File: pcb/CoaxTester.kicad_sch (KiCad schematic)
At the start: 20 parts

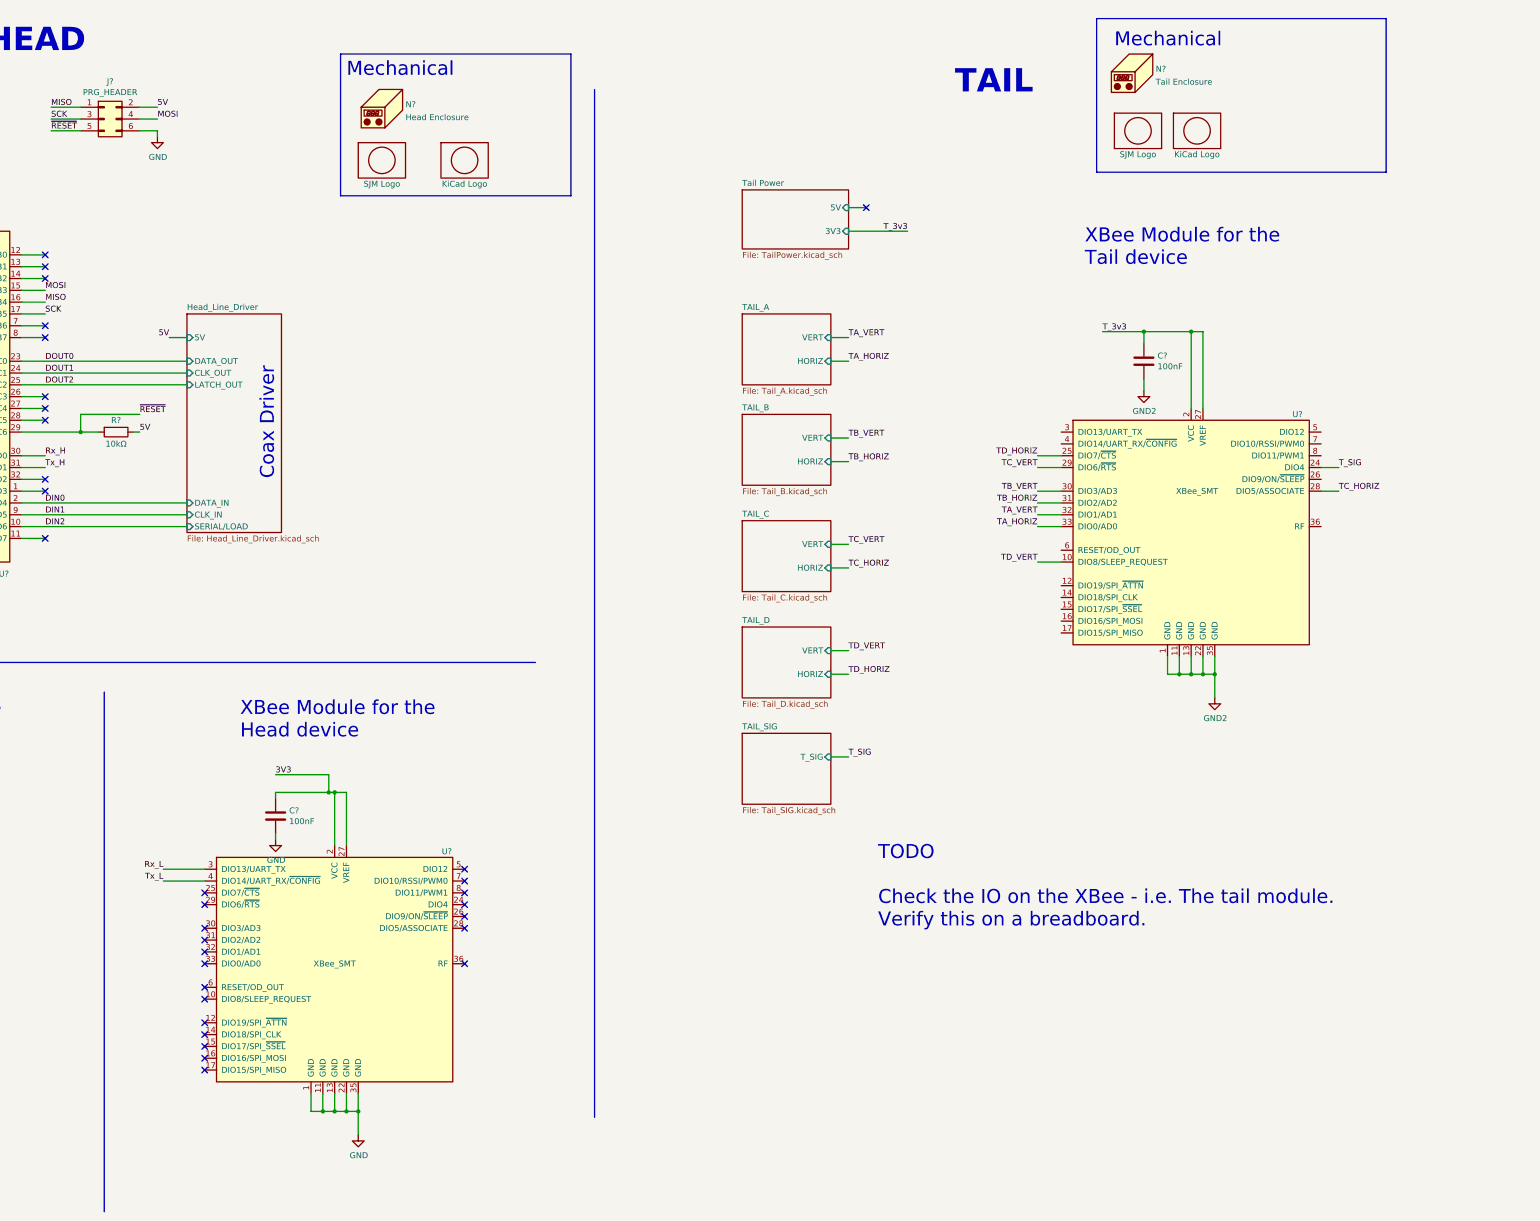
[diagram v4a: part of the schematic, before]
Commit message: Proof of concept for XBee tail unit. Correction to XBee symbol
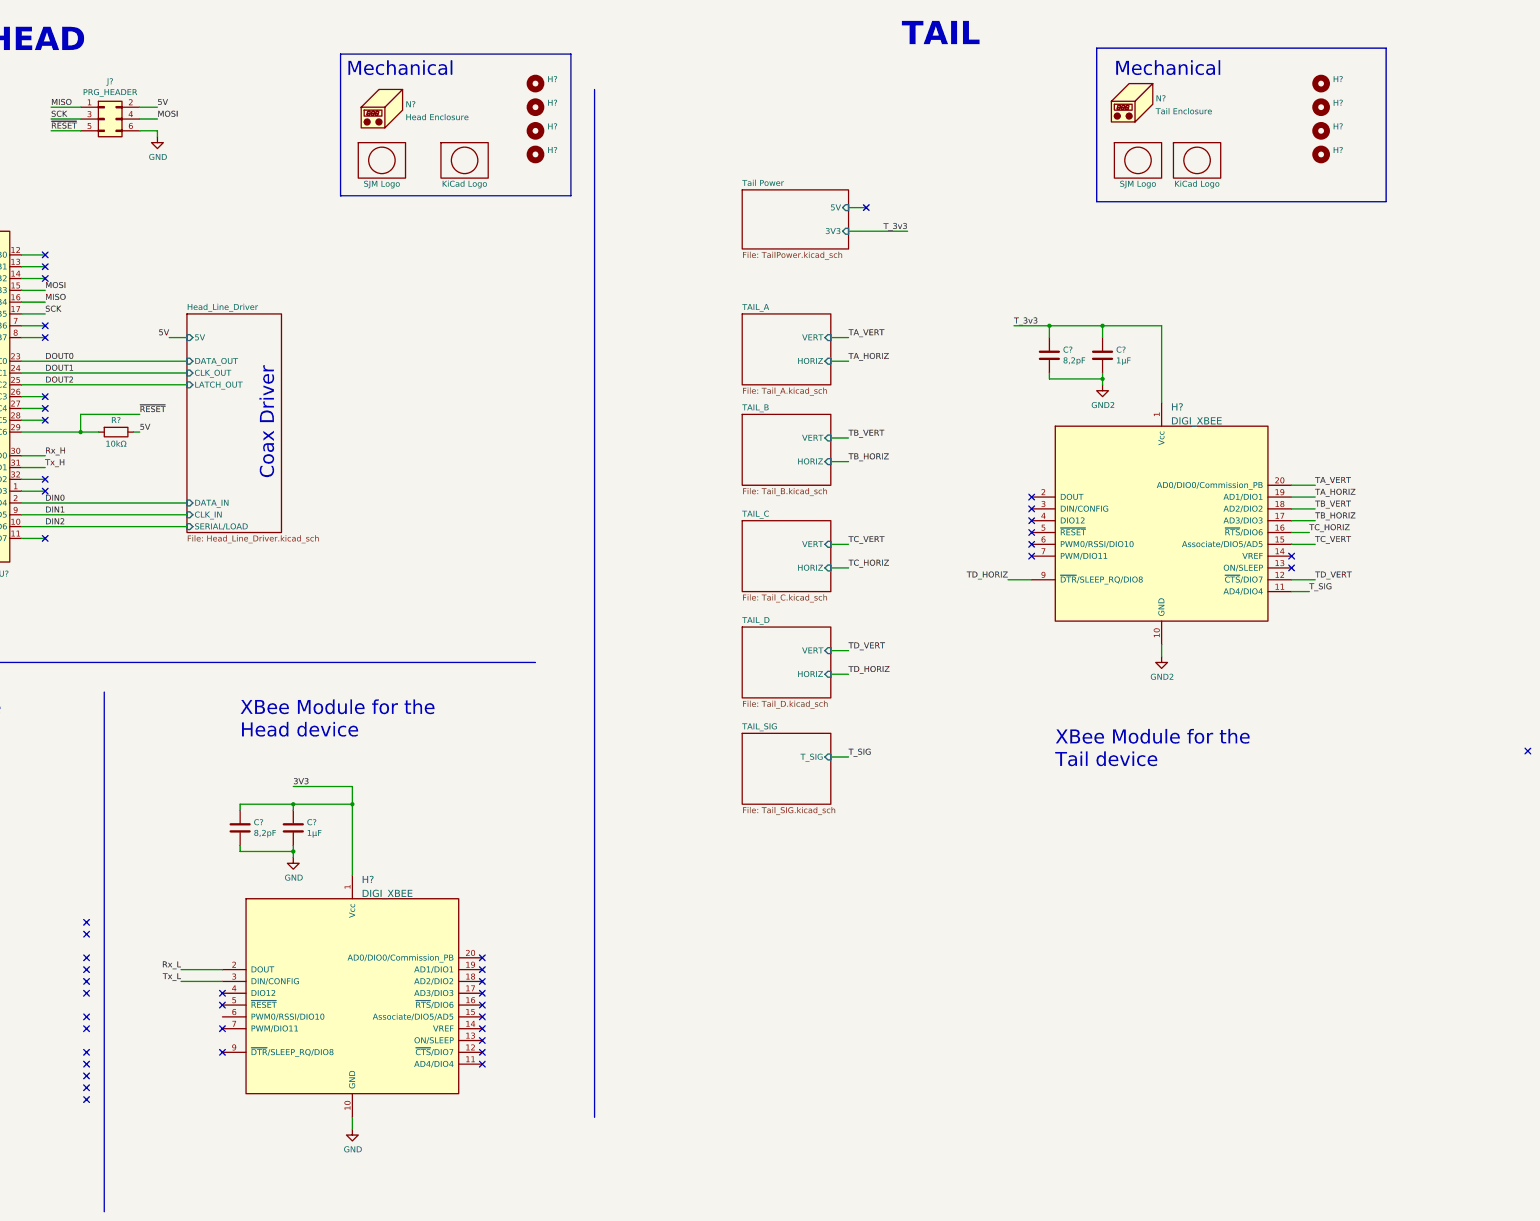
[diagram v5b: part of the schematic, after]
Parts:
- removed C?: 100nF, Capacitor_SMD:C_0805_2012Metric, symbol Device:C
- removed U? (x2): XBee_SMT, RF_Module:Digi_XBee_SMT, symbol RF_ZigBee:XBee_SMT
- added C?: 1μF, Capacitor_SMD:C_0805_2012Metric, symbol Device:C
- added C? (x2): 8,2pF, Capacitor_SMD:C_0805_2012Metric, symbol Device:C
- added H? (x8): MountingHole, MountingHole:MountingHole_3.2mm_M3, symbol Mechanical:MountingHole
- added H? (x2): DIGI_XBEE, symbol XBee-Adapter:DIGI_XBEE
- C?: value 100nF -> 1μF
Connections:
- net 3V3: now also C?.1, H?.1 (Vcc)
- net GND: now also C?.2, H?.10 (GND)
- net GND2: now also C?.2, C?.2, H?.10 (GND)
- net Rx_L: now also H?.2 (DOUT)
- net TA_HORIZ: now also H?.19 (AD1/DIO1)
- net TA_VERT: now also H?.20 (AD0/DIO0/Commission_PB)
- net TB_HORIZ: now also H?.17 (AD3/DIO3)
- net TB_VERT: now also H?.18 (AD2/DIO2)
- net TC_HORIZ: now also H?.16 (~{RTS}/DIO6)
- net TC_VERT: now also H?.15 (Associate/DIO5/AD5)
- net TD_HORIZ: now also H?.9 (~{DTR}/SLEEP_RQ/DIO8)
- net TD_VERT: now also H?.12 (~{CTS}/DIO7)
- net T_3v3: now also C?.1, C?.1, H?.1 (Vcc)
- net T_SIG: now also H?.11 (AD4/DIO4)
- net Tx_L: now also H?.3 (DIN/CONFIG)
- no-connect marks 35 -> 51
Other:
- note removed: "TODO Check the IO on the XBee - i.e. The tail module. Verify this on a breadboard."
- moved on the sheet: C?, N?

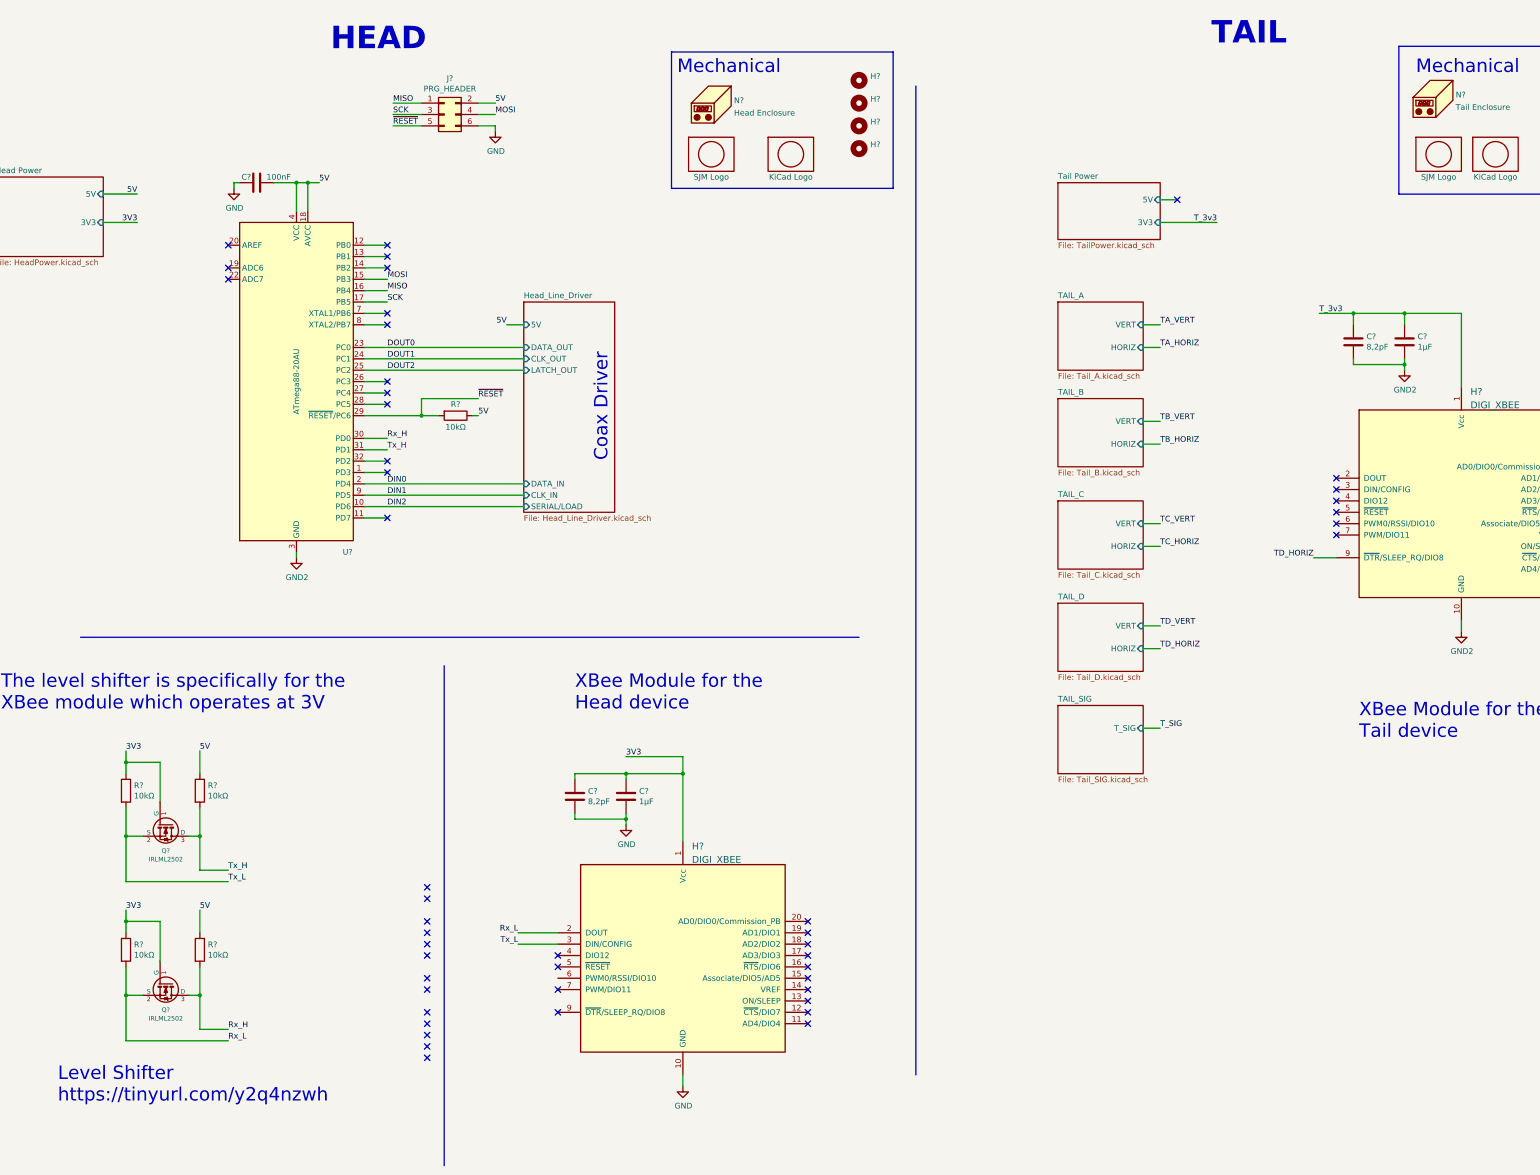
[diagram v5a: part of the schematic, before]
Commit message: Updates to the schematic for XBee
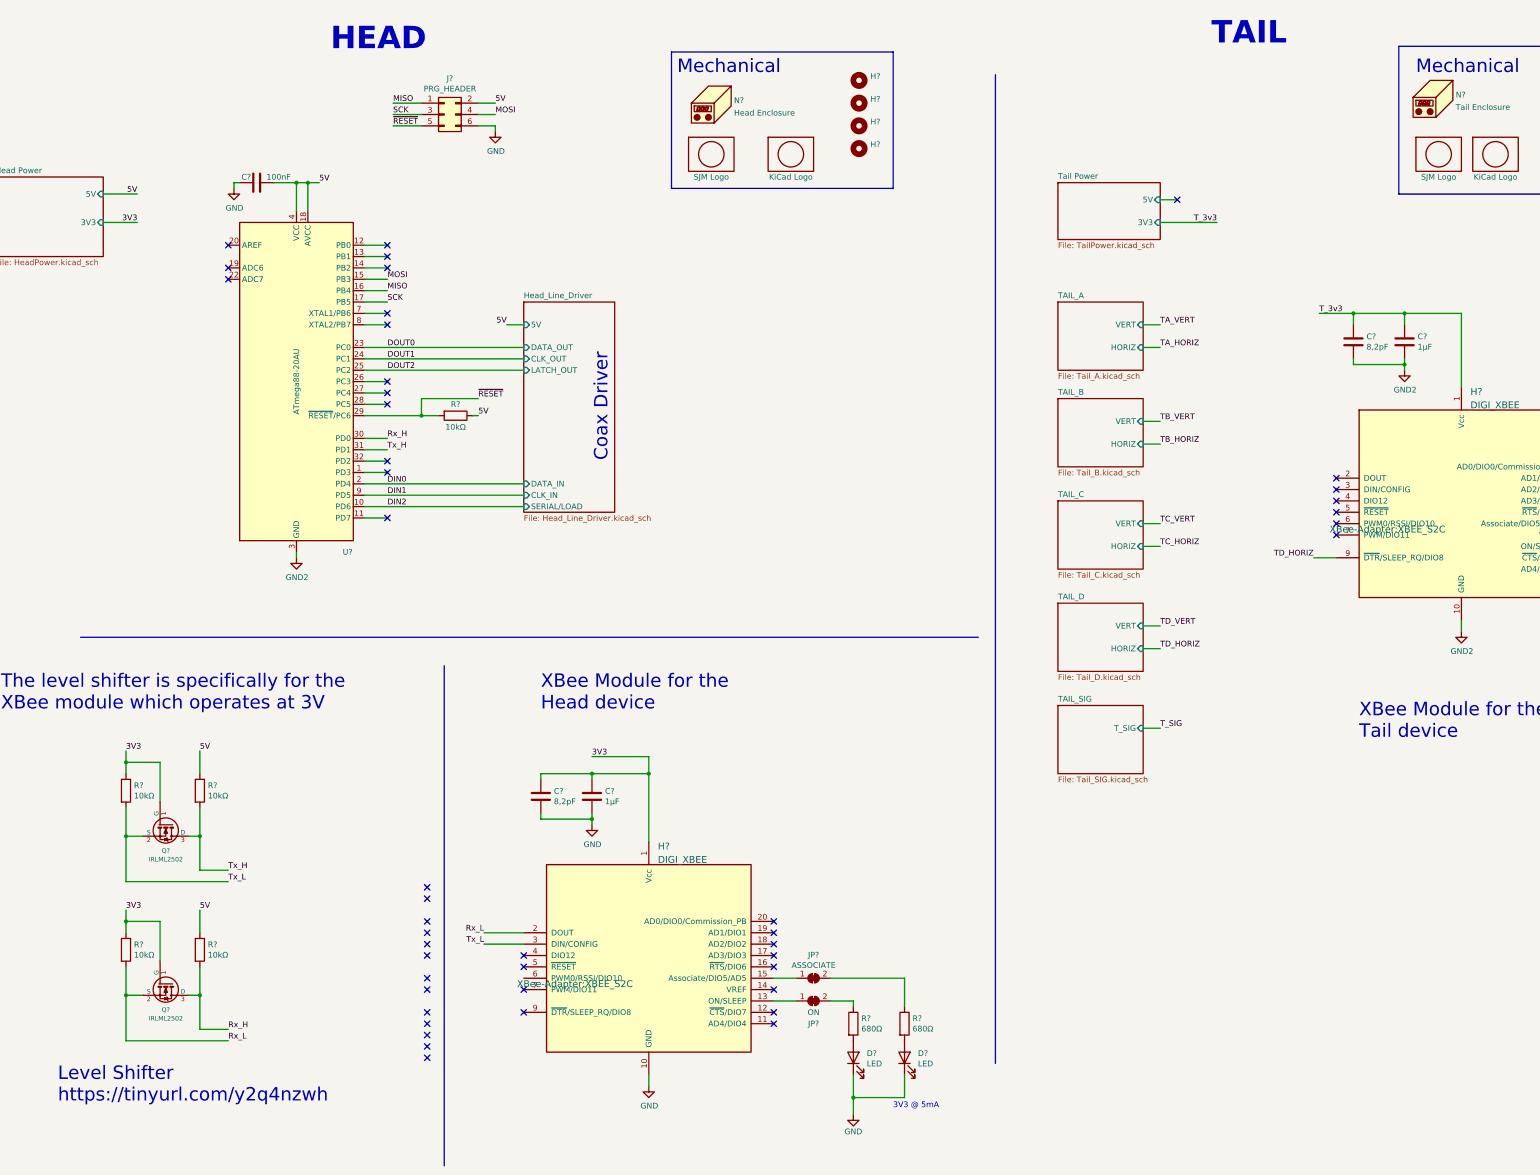
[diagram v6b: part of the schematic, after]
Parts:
- added D? (x2): LED, LED_SMD:LED_0805_2012Metric, symbol Device:LED
- added JP?: ASSOCIATE, Jumper:SolderJumper-2_P1.3mm_Bridged_RoundedPad1.0x1.5mm, symbol Jumper:SolderJumper_2_Bridged
- added JP?: ON, Jumper:SolderJumper-2_P1.3mm_Bridged_RoundedPad1.0x1.5mm, symbol Jumper:SolderJumper_2_Bridged
- added R? (x2): 680Ω, Resistor_SMD:R_0805_2012Metric, symbol Device:R
- H? (x2): footprint (none) -> XBee-Adapter:XBEE_S2C
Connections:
- net GND: now also D?.1 (K), D?.1 (K)
- net at H?.13 (ON/SLEEP): now also JP?.1 (A)
- net at H?.15 (Associate/DIO5/AD5): now also JP?.1 (A)
- new net: D?.2 (A), R?.2 (x2)
- new net: JP?.2 (B), R?.1 (x2)
- no-connect marks 51 -> 49
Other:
- note added: "3V3 @ 5mA"
- moved on the sheet: C?, H?
